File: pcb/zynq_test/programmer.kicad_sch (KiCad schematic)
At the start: 40 parts, among them J601 USB_B_Micro, J602 Conn_01x06_Pin, U601 FT2232HL, U602 93LCxxB, U603 DSC1001CI2-012

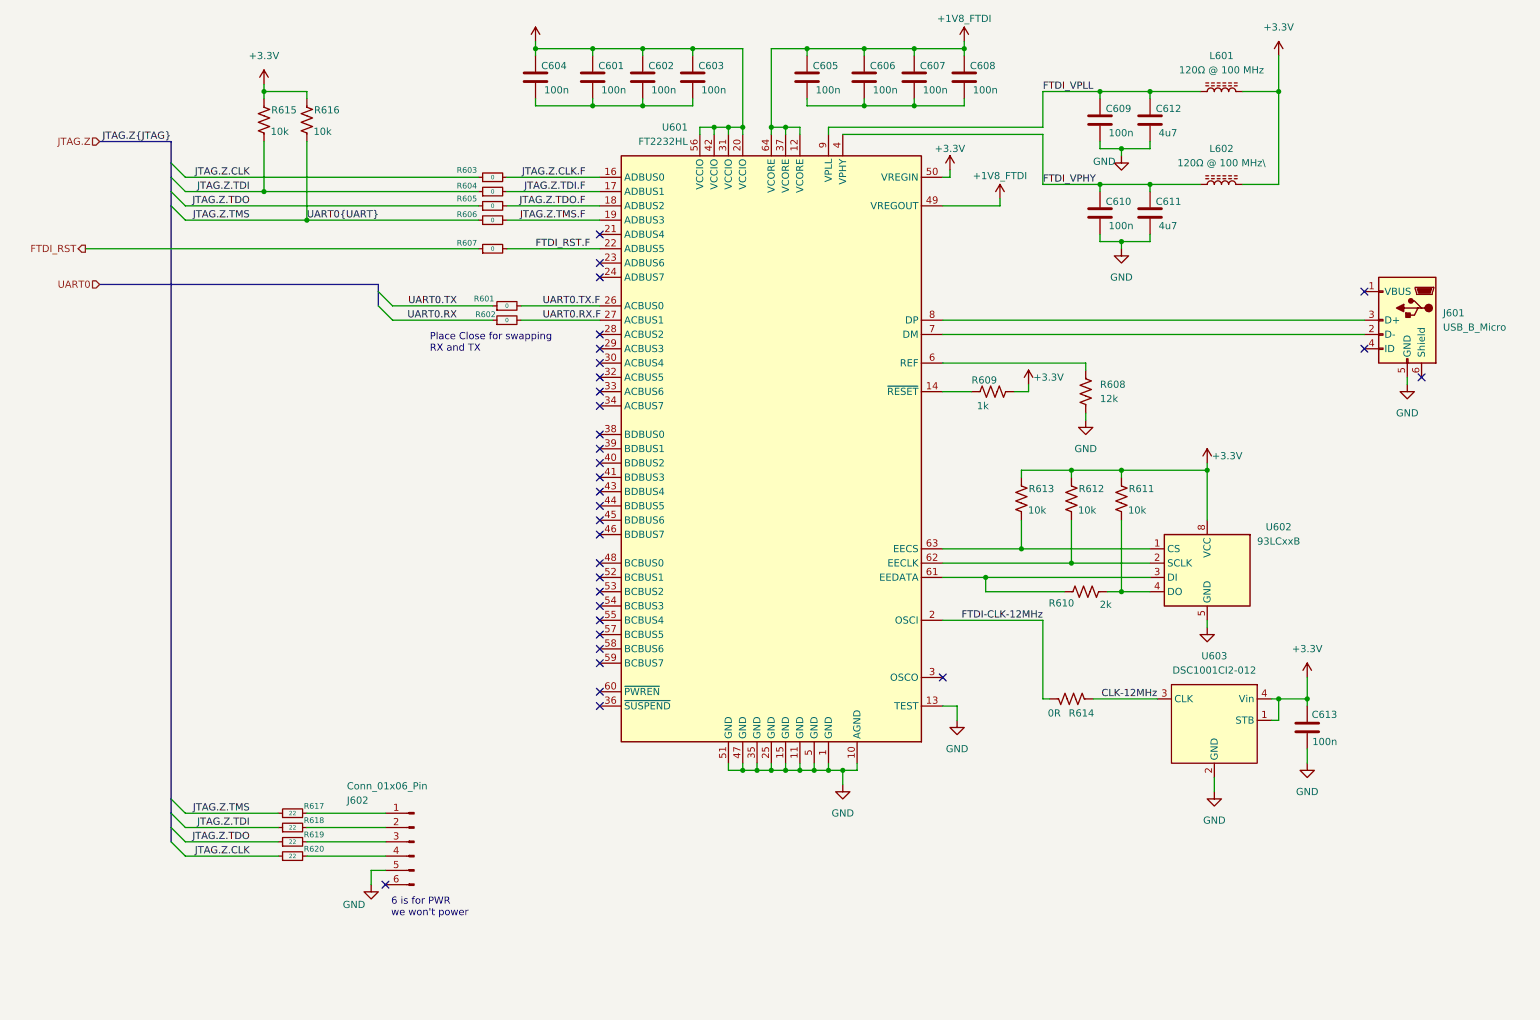
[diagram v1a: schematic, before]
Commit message: Finished Ethernet, swapped FTDI chip for QFN
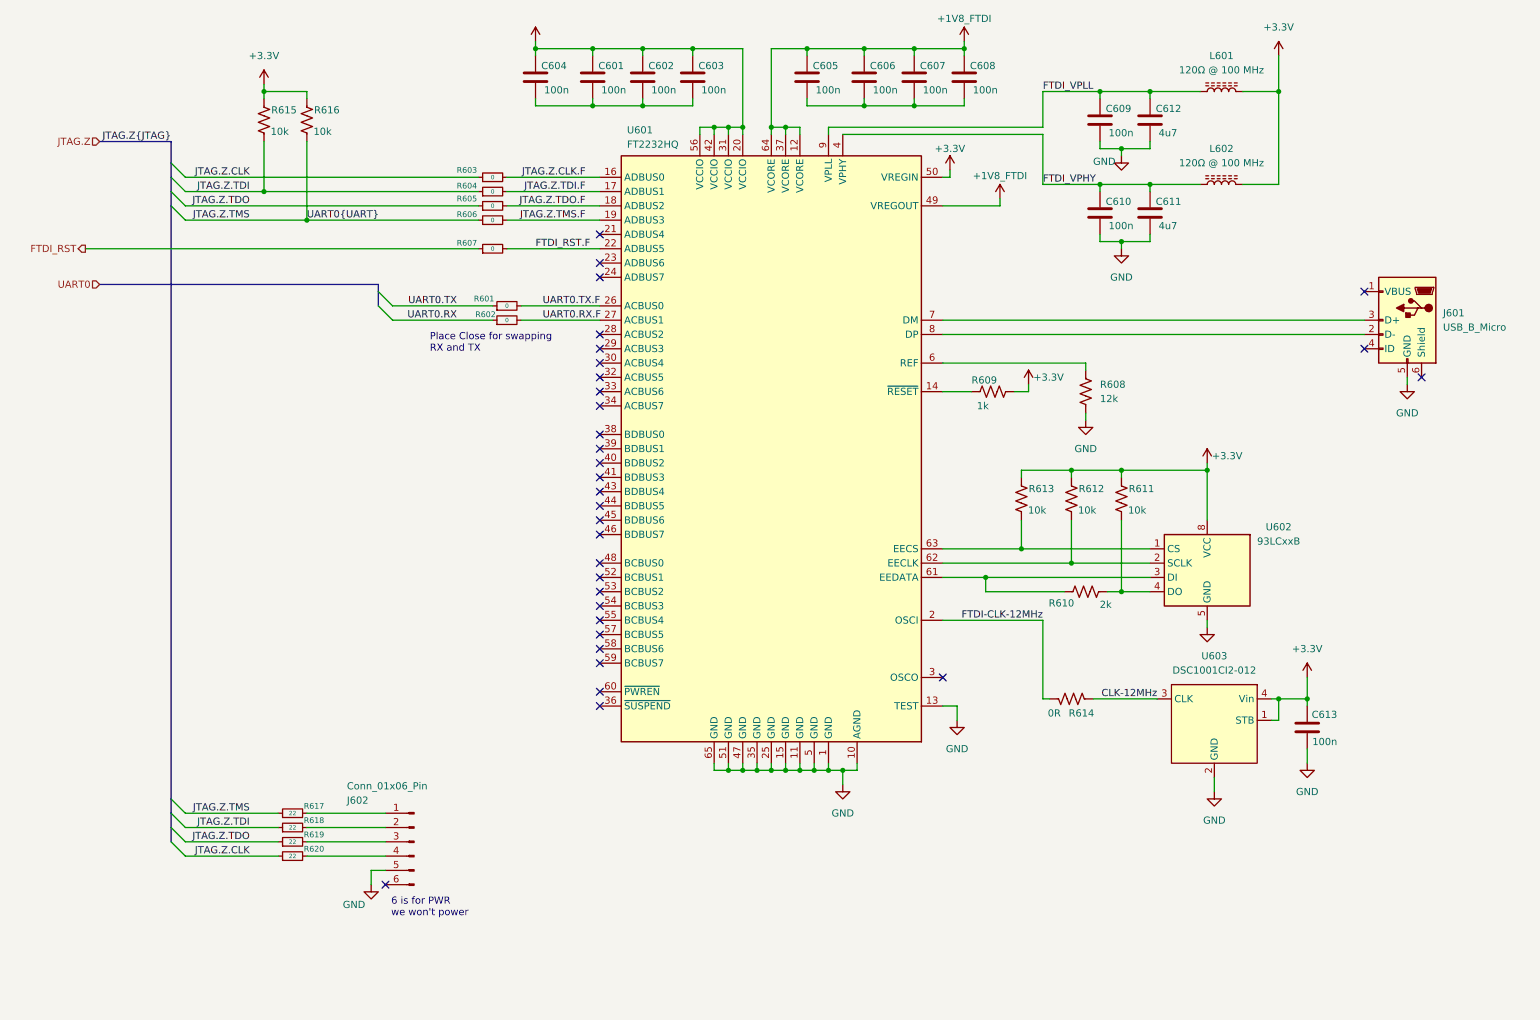
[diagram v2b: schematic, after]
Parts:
- removed U601: FT2232HL, Package_QFP:LQFP-64_10x10mm_P0.5mm, symbol Interface_USB:FT2232HL
- added U601: FT2232HQ, Package_DFN_QFN:QFN-64-1EP_9x9mm_P0.5mm_EP4.35x4.35mm, symbol Interface_USB:FT2232HQ
- L602: value 120Ω @ 100 MHz\ -> 120Ω @ 100 MHz
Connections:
- net +1V8_FTDI: now also U601.12 (VCORE), U601.37 (VCORE), U601.49 (VREGOUT), U601.64 (VCORE)
- net +3.3V: now also U601.20 (VCCIO), U601.31 (VCCIO), U601.42 (VCCIO), U601.50 (VREGIN), U601.56 (VCCIO)
- net FTDI-CLK-12MHz: now also U601.2 (OSCI)
- net FTDI_RST.F: now also U601.22 (ADBUS5)
- net FTDI_VPHY: now also U601.4 (VPHY)
- net FTDI_VPLL: now also U601.9 (VPLL)
- net GND: now also U601.1 (GND), U601.10 (AGND), U601.11 (GND), U601.13 (TEST), U601.15 (GND), U601.25 (GND), U601.35 (GND), U601.47 (GND), U601.5 (GND), U601.51 (GND), U601.65 (GND)
- net JTAG.Z.CLK.F: now also U601.16 (ADBUS0)
- net JTAG.Z.TDI.F: now also U601.17 (ADBUS1)
- net JTAG.Z.TDO.F: now also U601.18 (ADBUS2)
- net JTAG.Z.TMS.F: now also U601.19 (ADBUS3)
- net UART0.RX.F: now also U601.27 (ACBUS1)
- net UART0.TX.F: now also U601.26 (ACBUS0)
- net at R610.1, U602.3 (DI): now also U601.61 (EEDATA)
- net at R608.1: now also U601.6 (REF)
- net at J601.2 (D-): now also U601.8 (DP)
- net at J601.3 (D+): now also U601.7 (DM)
- net at R612.1, U602.2 (SCLK): now also U601.62 (EECLK)
- net at R609.1: now also U601.14 (~{RESET})
- net at R613.1, U602.1 (CS): now also U601.63 (EECS)
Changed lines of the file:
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@@
 	)
 	(junction
+		(at 137.16 152.4)
+		(diameter 0)
+		(color 0 0 0 0)
+	)
+	(junction
 		(at 147.32 38.1)
 		(diameter 0)
@@
 	(wire
 		(pts
+			(xy 134.62 151.13) (xy 134.62 152.4)
+		)
+		(stroke
+			(width 0)
+			(type default)
+		)
+	)
+	(wire
+		(pts
 			(xy 102.87 24.13) (xy 102.87 25.4)
 		)
@@
 	(wire
 		(pts
+			(xy 134.62 152.4) (xy 137.16 152.4)
+		)
+		(stroke
+			(width 0)
+			(type default)
+		)
+	)
+	(wire
+		(pts
 			(xy 73.66 170.18) (xy 76.2 170.18)
 		)
@@
 			)
 		)
-		(property "Value" "120Ω @ 100 MHz\\"
+		(property "Value" "120Ω @ 100 MHz"
 			(at 224.79 44.45 90)
 			(effects
@@
 	)
 	(symbol
-		(lib_id "Interface_USB:FT2232HL")
+		(lib_id "Device:R_Small")
+		(at 95.25 54.61 90)
+		(unit 1)
+		(exclude_from_sim no)
+		(in_bom yes)
+		(on_board yes)
+		(dnp no)
+		(property "Reference" "R606"
+			(at 90.678 53.594 90)
+			(effects
+				(font
+					(size 1.016 1.016)
+				)
+			)
+		)
+		(property "Value" "0"
+			(at 95.25 54.61 90)
+			(effects
+				(font
+					(size 0.762 0.762)
+				)
+			)
+		)
+		(property "Footprint" ""
+			(at 95.25 54.61 0)
+			(effects
+				(font
+					(size 1.27 1.27)
+				)
+				(hide yes)
+			)
+		)
+		(property "Datasheet" "~"
+			(at 95.25 54.61 0)
+			(effects
+				(font
+					(size 1.27 1.27)
+				)
+				(hide yes)
+			)
+		)
+		(property "Description" "Resistor, small symbol"
+			(at 95.25 54.61 0)
+			(effects
+				(font
+					(size 1.27 1.27)
+				)
+				(hide yes)
+			)
+		)
+		(pin "2"
+		)
+		(pin "1"
+		)
+		(instances
+			(project "zynq_test"
+				(path "/0637578d-4ce5-4d31-b973-2de977269ea5/cbe65b94-50f2-402b-8037-053235586035"
+					(reference "R606")
+					(unit 1)
+				)
+			)
+		)
+	)
+	(symbol
+		(lib_id "Interface_USB:FT2232HQ")
 		(at 144.78 95.25 0)
 		(mirror y)
@@
 		(dnp no)
 		(property "Reference" "U601"
-			(at 129.9367 38.1 0)
+			(at 119.126 38.608 0)
 			(effects
 				(font
 					(size 1.27 1.27)
 				)
-				(justify left)
+				(justify right)
 			)
 		)
-		(property "Value" "FT2232HL"
-			(at 129.9367 40.64 0)
+		(property "Value" "FT2232HQ"
+			(at 119.126 41.148 0)
 			(effects
 				(font
 					(size 1.27 1.27)
 				)
-				(justify left)
+				(justify right)
 			)
 		)
-		(property "Footprint" "Package_QFP:LQFP-64_10x10mm_P0.5mm"
+		(property "Footprint" "Package_DFN_QFN:QFN-64-1EP_9x9mm_P0.5mm_EP4.35x4.35mm"
 			(at 144.78 95.25 0)
 			(effects
@@
 			)
 		)
-		(property "Description" "Hi Speed Double Channel USB UART/FIFO, LQFP-64"
+		(property "Description" "Hi Speed Double Channel USB UART/FIFO, QFN-64"
 			(at 144.78 95.25 0)
 			(effects
@@
 			)
 		)
-		(pin "3"
-		)
-		(pin "5"
+		(pin "25"
 		)
-		(pin "50"
+		(pin "11"
 		)
-		(pin "49"
+		(pin "42"
 		)
-		(pin "7"
+		(pin "64"
 		)
-		(pin "8"
+		(pin "17"
 		)
 		(pin "6"
 		)
-		(pin "63"
-		)
 		(pin "14"
 		)
-		(pin "62"
-		)
 		(pin "61"
 		)
-		(pin "2"
+		(pin "3"
 		)
-		(pin "13"
+		(pin "9"
 		)
-		(pin "4"
+		(pin "63"
 		)
-		(pin "10"
+		(pin "1"
 		)
-		(pin "9"
+		(pin "5"
 		)
-		(pin "1"
+		(pin "37"
+		)
+		(pin "10"
 		)
 		(pin "20"
 		)
-		(pin "25"
+		(pin "47"
 		)
-		(pin "28"
+		(pin "12"
 		)
-		(pin "31"
+		(pin "15"
 		)
-		(pin "22"
+		(pin "51"
 		)
-		(pin "33"
+		(pin "65"
 		)
-		(pin "64"
+		(pin "2"
 		)
-		(pin "38"
+		(pin "62"
 		)
-		(pin "42"
+		(pin "13"
 		)
-		(pin "39"
+		(pin "4"
 		)
-		(pin "15"
+		(pin "35"
 		)
-		(pin "18"
+		(pin "31"
 		)
-		(pin "12"
+		(pin "56"
 		)
-		(pin "37"
+		(pin "16"
 		)
-		(pin "19"
+		(pin "26"
 		)
-		(pin "21"
+		(pin "24"
 		)
-		(pin "51"
+		(pin "28"
 		)
-		(pin "47"
+		(pin "48"
 		)
-		(pin "26"
+		(pin "32"
 		)
-		(pin "11"
+		(pin "58"
 		)
-		(pin "16"
+		(pin "44"
 		)
-		(pin "17"
+		(pin "36"
 		)
-		(pin "56"
+		(pin "19"
 		)
-		(pin "35"
+		(pin "22"
 		)
 		(pin "23"
 		)
-		(pin "24"
-		)
-		(pin "27"
-		)
-		(pin "29"
+		(pin "39"
 		)
-		(pin "30"
+		(pin "41"
 		)
-		(pin "32"
+		(pin "33"
 		)
 		(pin "34"
 		)
-		(pin "43"
+		(pin "45"
 		)
 		(pin "46"
 		)
-		(pin "52"
+		(pin "54"
 		)
-		(pin "57"
+		(pin "29"
 		)
-		(pin "40"
+		(pin "18"
 		)
-		(pin "41"
+		(pin "30"
 		)
-		(pin "44"
+		(pin "43"
 		)
-		(pin "45"
+		(pin "27"
 		)
-		(pin "48"
+		(pin "38"
+		)
+		(pin "21"
+		)
+		(pin "40"
 		)
 		(pin "53"
 		)
-		(pin "54"
+		(pin "52"
 		)
 		(pin "55"
 		)
-		(pin "36"
-		)
-		(pin "60"
+		(pin "57"
 		)
 		(pin "59"
 		)
-		(pin "58"
-		)
-		(instances
-			(project ""
-				(path "/0637578d-4ce5-4d31-b973-2de977269ea5/cbe65b94-50f2-402b-8037-053235586035"
-					(reference "U601")
-					(unit 1)
-				)
-			)
-		)
-	)
-	(symbol
-		(lib_id "Device:R_Small")
-		(at 95.25 54.61 90)
-		(unit 1)
-		(exclude_from_sim no)
-		(in_bom yes)
-		(on_board yes)
-		(dnp no)
-		(property "Reference" "R606"
-			(at 90.678 53.594 90)
-			(effects
-				(font
-					(size 1.016 1.016)
-				)
-			)
-		)
-		(property "Value" "0"
-			(at 95.25 54.61 90)
-			(effects
-				(font
-					(size 0.762 0.762)
-				)
-			)
-		)
-		(property "Footprint" ""
-			(at 95.25 54.61 0)
-			(effects
-				(font
-					(size 1.27 1.27)
-				)
-				(hide yes)
-			)
+		(pin "60"
 		)
-		(property "Datasheet" "~"
-			(at 95.25 54.61 0)
-			(effects
-				(font
-					(size 1.27 1.27)
-				)
-				(hide yes)
-			)
+		(pin "50"
 		)
-		(property "Description" "Resistor, small symbol"
-			(at 95.25 54.61 0)
-			(effects
-				(font
-					(size 1.27 1.27)
-				)
-				(hide yes)
-			)
+		(pin "8"
 		)
-		(pin "2"
+		(pin "49"
 		)
-		(pin "1"
+		(pin "7"
 		)
 		(instances
-			(project "zynq_test"
+			(project ""
 				(path "/0637578d-4ce5-4d31-b973-2de977269ea5/cbe65b94-50f2-402b-8037-053235586035"
-					(reference "R606")
+					(reference "U601")
 					(unit 1)
 				)

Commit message: Finished HDMI
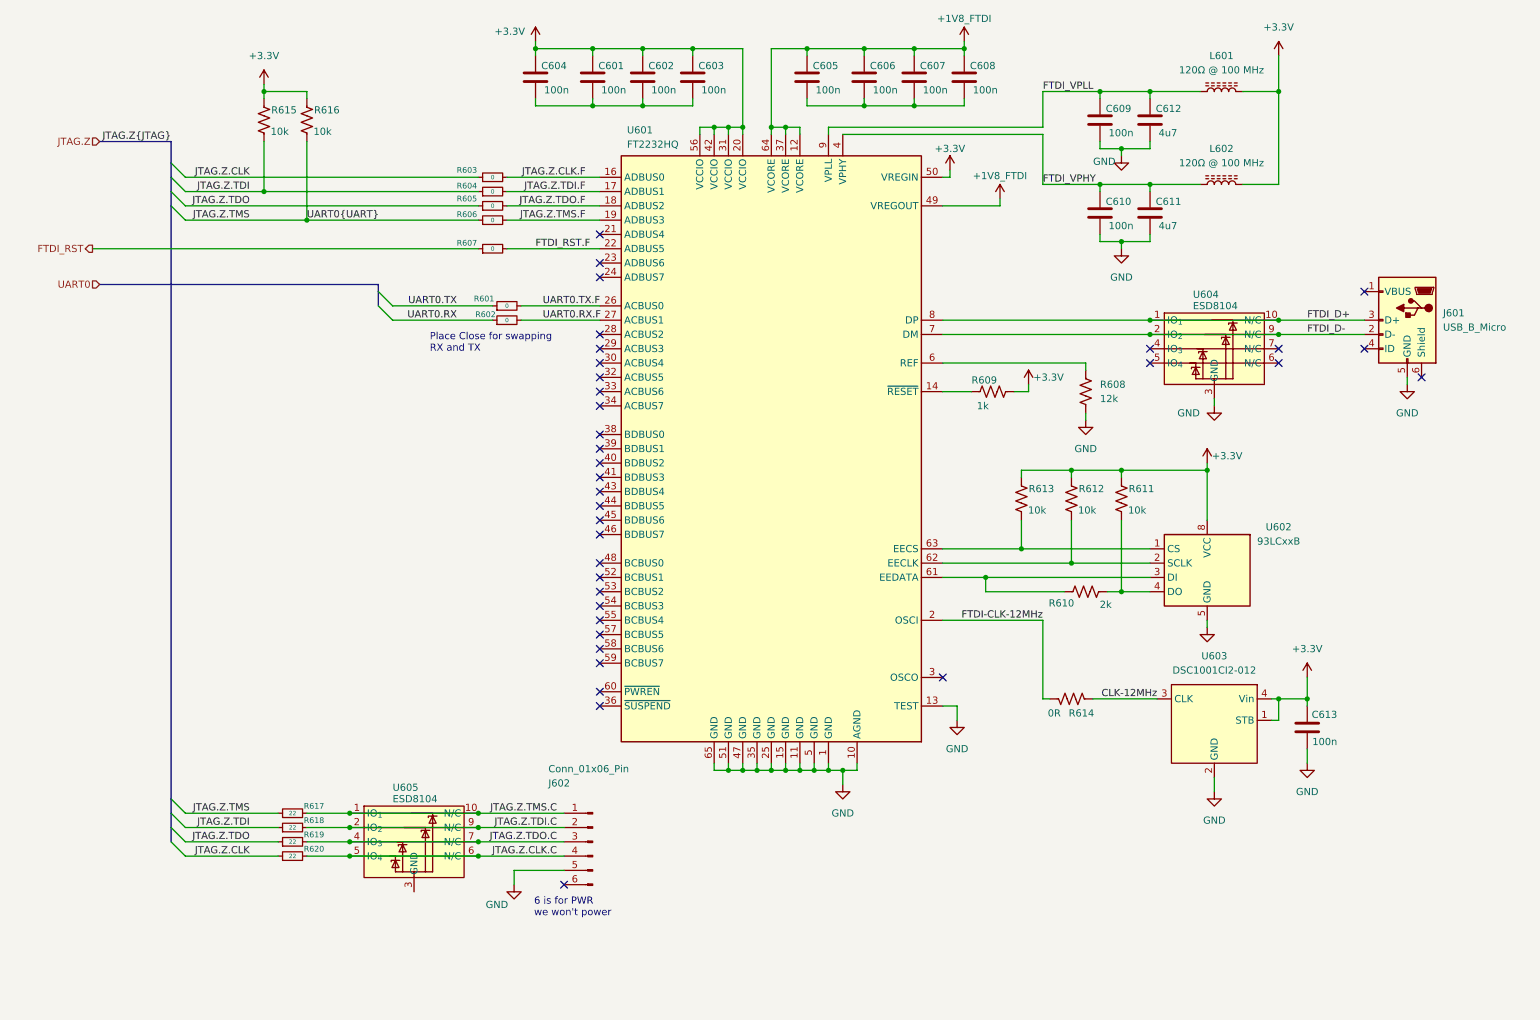
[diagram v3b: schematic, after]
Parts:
- added U604, U605: ESD8104, symbol other:ESD8104
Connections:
- net GND: now also U604.3 (GND)
- net JTAG.Z.TDO.C: now reaches J602.3 (Pin_3), R619.2
- net JTAG.Z.TDO.C: now also U605.4 (IO_{3}), U605.7 (N/C)
- net FTDI_D+: now reaches U601.8 (DP)
- net FTDI_D+: now also J601.3 (D+), U604.1 (IO_{1}), U604.10 (N/C); no longer J601.2 (D-)
- net FTDI_D-: now reaches U601.7 (DM)
- net FTDI_D-: now also J601.2 (D-), U604.2 (IO_{2}), U604.9 (N/C); no longer J601.3 (D+)
- net JTAG.Z.TMS.C: now reaches J602.1 (Pin_1), R617.2
- net JTAG.Z.TMS.C: now also U605.1 (IO_{1}), U605.10 (N/C)
- net JTAG.Z.TDI.C: now reaches J602.2 (Pin_2), R618.2
- net JTAG.Z.TDI.C: now also U605.2 (IO_{2}), U605.9 (N/C)
- net JTAG.Z.CLK.C: now reaches J602.4 (Pin_4), R620.2
- net JTAG.Z.CLK.C: now also U605.5 (IO_{4}), U605.6 (N/C)
- no-connect marks 32 -> 36
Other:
- moved on the sheet: J602
